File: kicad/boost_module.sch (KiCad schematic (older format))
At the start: 44 parts, among them Q1 NVTFS5C466NL, Q2 NVTFS5C466NL, Q3 NVTFS5C466NL, Q4 NVTFS5C466NL, SW1 ON/OFF, SW2 Select_Vout, U1 LM34936-Q1

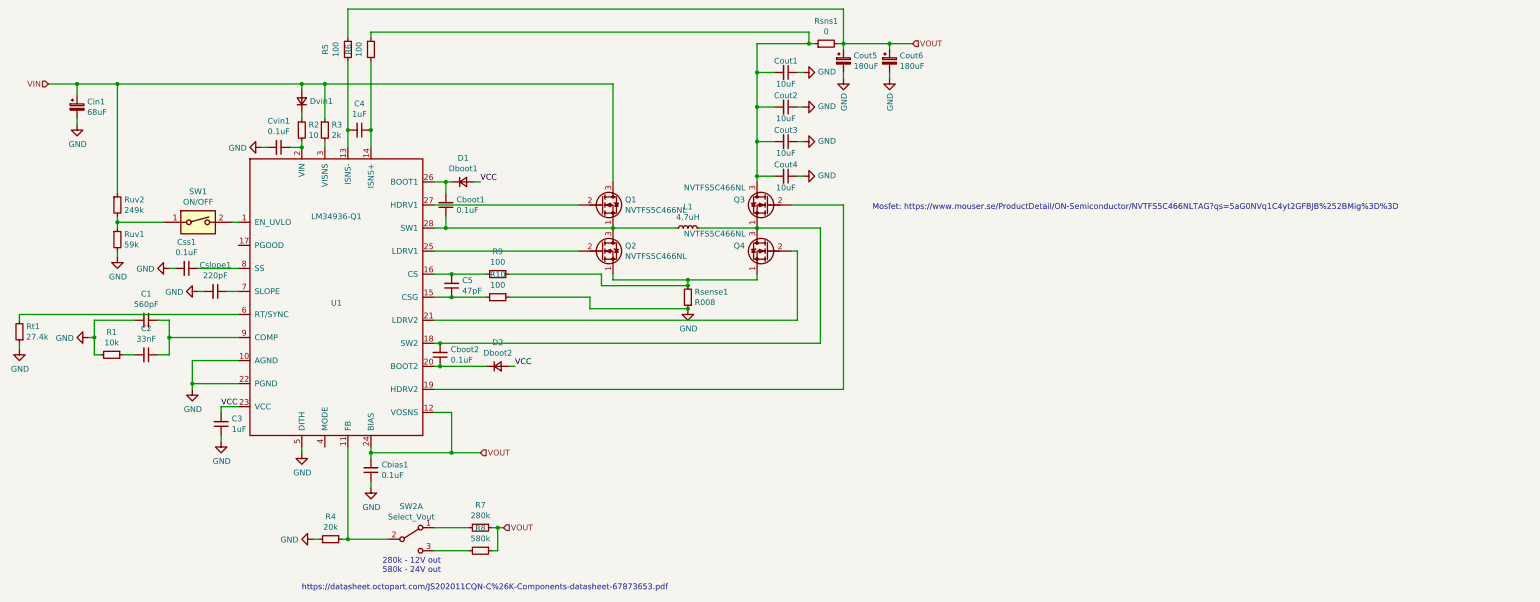
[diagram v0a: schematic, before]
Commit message: Updated schematic
Made some error with first rev, the found error are now corrected.
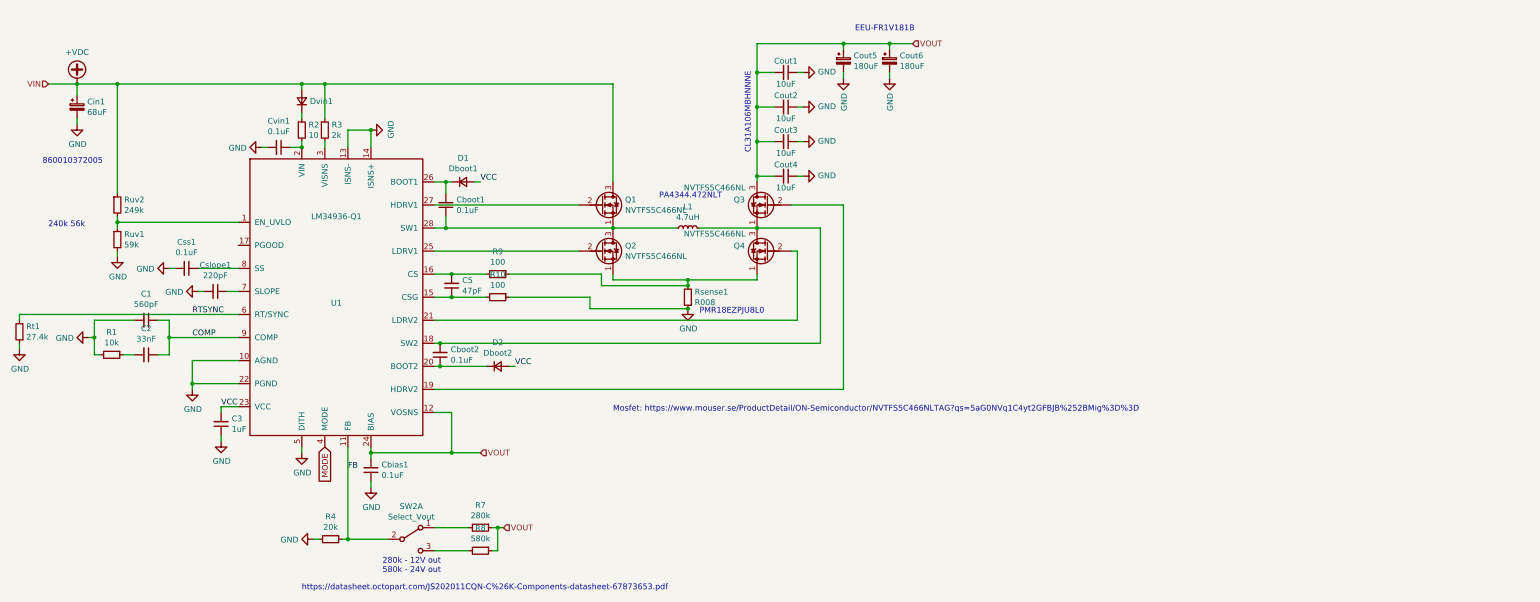
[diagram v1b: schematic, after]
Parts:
- removed C4: 1uF, symbol Device:C_Small
- removed R5, R6: 100, Resistor_SMD:R_0603_1608Metric, symbol Device:R_Small
- removed Rsns1: 0, symbol Device:R_Small
- removed SW1: ON/OFF, symbol Switch:SW_DIP_x01
- C1, C2, C3, C5, Cbias1, Cboot1, Cboot2, Cslope1, Css1, Cvin1: footprint (none) -> Capacitor_SMD:C_0603_1608Metric
- Cin1: footprint (none) -> Capacitor_THT:CP_Radial_D5.0mm_P2.00mm
- Cout1, Cout2, Cout3, Cout4: footprint (none) -> Capacitor_SMD:C_1206_3216Metric
- Cout5, Cout6: footprint (none) -> Capacitor_THT:CP_Radial_D8.0mm_P3.50mm
- Dvin1: footprint (none) -> Diode_SMD:D_SOD-123
- L1: footprint (none) -> inductor:Pulse_PA4344.XXXNLT
- Q1, Q2, Q3, Q4: footprint (none) -> mosfet:8-PowerWDFN
- Rsense1: footprint (none) -> Resistor_SMD:R_1206_3216Metric
- Rt1, Ruv1, Ruv2: footprint (none) -> Resistor_SMD:R_0603_1608Metric
- SW2: footprint (none) -> Connector_JST:JST_XH_B3B-XH-A_1x03_P2.50mm_Vertical
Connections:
- net GND: now also U1.13 (ISNS-), U1.14 (ISNS+)
- net VOUT: now also Cout1.2, Cout2.2, Cout3.2, Cout4.2, Q3.3 (D)
- net at U1.1 (EN_UVLO): now also Ruv1.1, Ruv2.2
- net FB: now reaches R4.1, SW2.2 (B), U1.11 (FB)
- net MODE: now reaches U1.4 (MODE)
- net RTSYNC: now reaches Rt1.2, U1.6 (RT/SYNC)
- net COMP: now reaches C1.1, C2.1, U1.9 (COMP)
- net VIN renamed +VDC
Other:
- note added: "240k 56k\n"
- note added: "860010372005"
- note added: "CL31A106MBHNNNE"
- note added: "EEU-FR1V181B"
- note added: "PA4344.472NLT\n"
- note added: "PMR18EZPJU8L0"
